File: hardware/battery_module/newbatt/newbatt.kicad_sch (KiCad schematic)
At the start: 28 parts, among them J1 54-00164, J2 Conn_01x10, U1 BQ24210DQCR

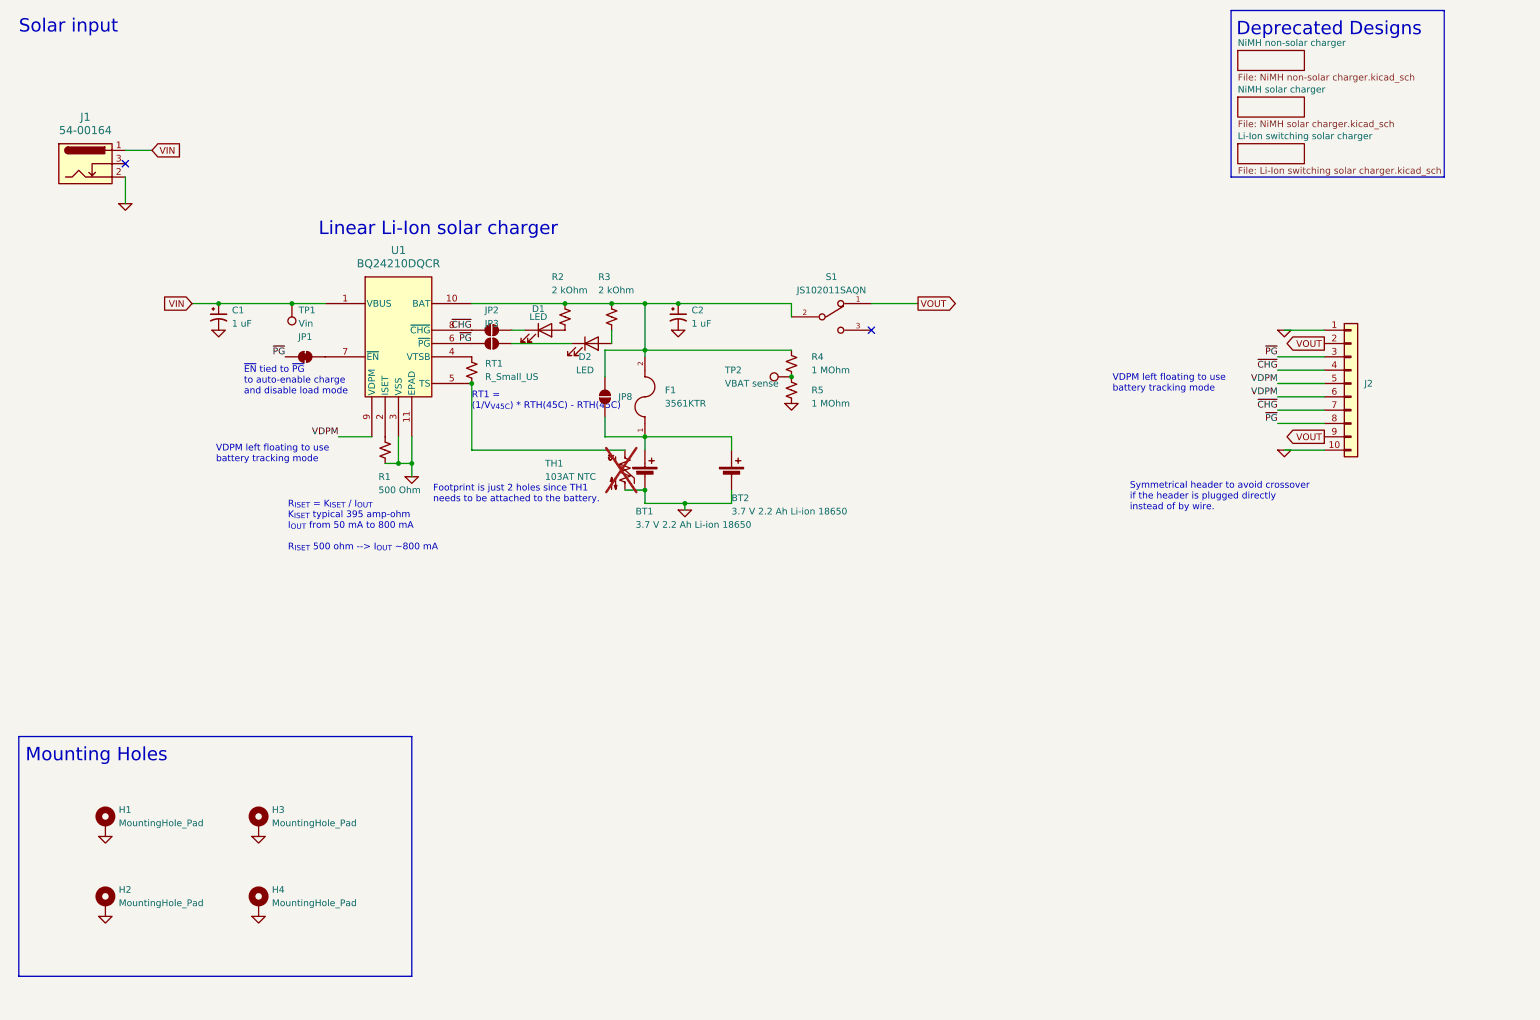
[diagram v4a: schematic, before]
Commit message: Updated BoM with LCSC, Digikey. Updated 18650 battery clip footprint with 67.2mm spacing for 65mm and 67mm cells
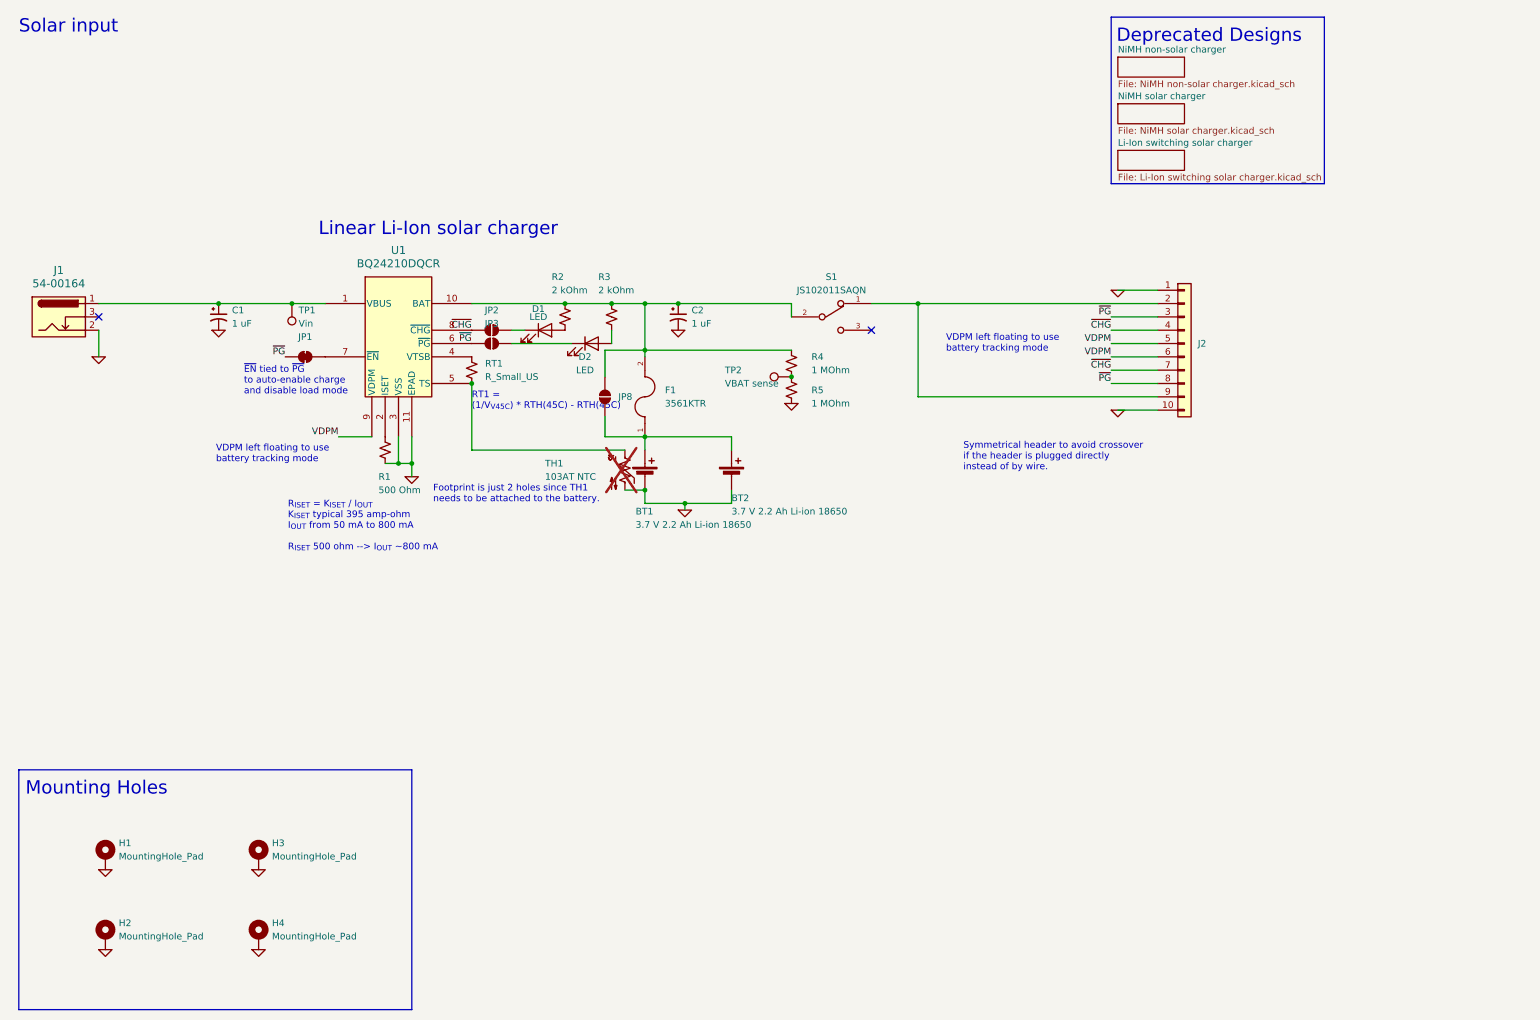
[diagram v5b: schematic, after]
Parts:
- BT1, BT2: footprint Keystone254TR:BAT_254TR -> Keystone254TR:BAT_254TR_67mm; Digikey (none) -> 36-254TR-ND; LCSC (none) -> C5498533; MFC (none) -> Keystone; MPN (none) -> 254TR; QTY (none) -> 4; REF (none) -> BT1, BT2
- F1: Digikey (none) -> 36-3561KTR-ND; LCSC (none) -> C3205939; MFC (none) -> Keystone; MPN (none) -> 3561KTR; QTY (none) -> 1; REF (none) -> F1
- J1: Digikey (none) -> 839-54-00164TR-ND; MFC (none) -> Tensility; MPN (none) -> 54-00164; QTY (none) -> 1; REF (none) -> J1
- J2: Digikey (none) -> S5485-ND; LCSC (none) -> C7327804; MFC (none) -> Sullins Connector Solutions; MPN (none) -> PPPC101LGBN-RC; QTY (none) -> 1; REF (none) -> J2
- S1: Digikey (none) -> 401-1999-2-ND; LCSC (none) -> C221660; MFC (none) -> C&K Switches; MPN (none) -> JS102011SAQN; QTY (none) -> 1; REF (none) -> S1
- TH1: Digikey (none) -> 4316-103AT-4-70374-ND; LCSC (none) -> C20583168; MFC (none) -> Semitec; MPN (none) -> 103AT-4-70374; QTY (none) -> 1; REF (none) -> TH1
- U1: Digikey (none) -> 296-BQ24210DQCRTR-ND; LCSC (none) -> C524795; MFC (none) -> Texas Instruments; MPN (none) -> BQ24210DQCR; QTY (none) -> 1; REF (none) -> U1
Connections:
- net VIN: no longer names the net of C1.1, J1.1, TP1.1, U1.1 (VBUS)
- net VOUT: no longer names the net of J2.2 (Pin_2), J2.9 (Pin_9), S1.1
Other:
- title: (none) -> ENTS Node Battery Module
- moved on the sheet: H1, H2, H3, H4, J1, J2

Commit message: Reviewed with John, updated VDPM and resistor values and barrel jack
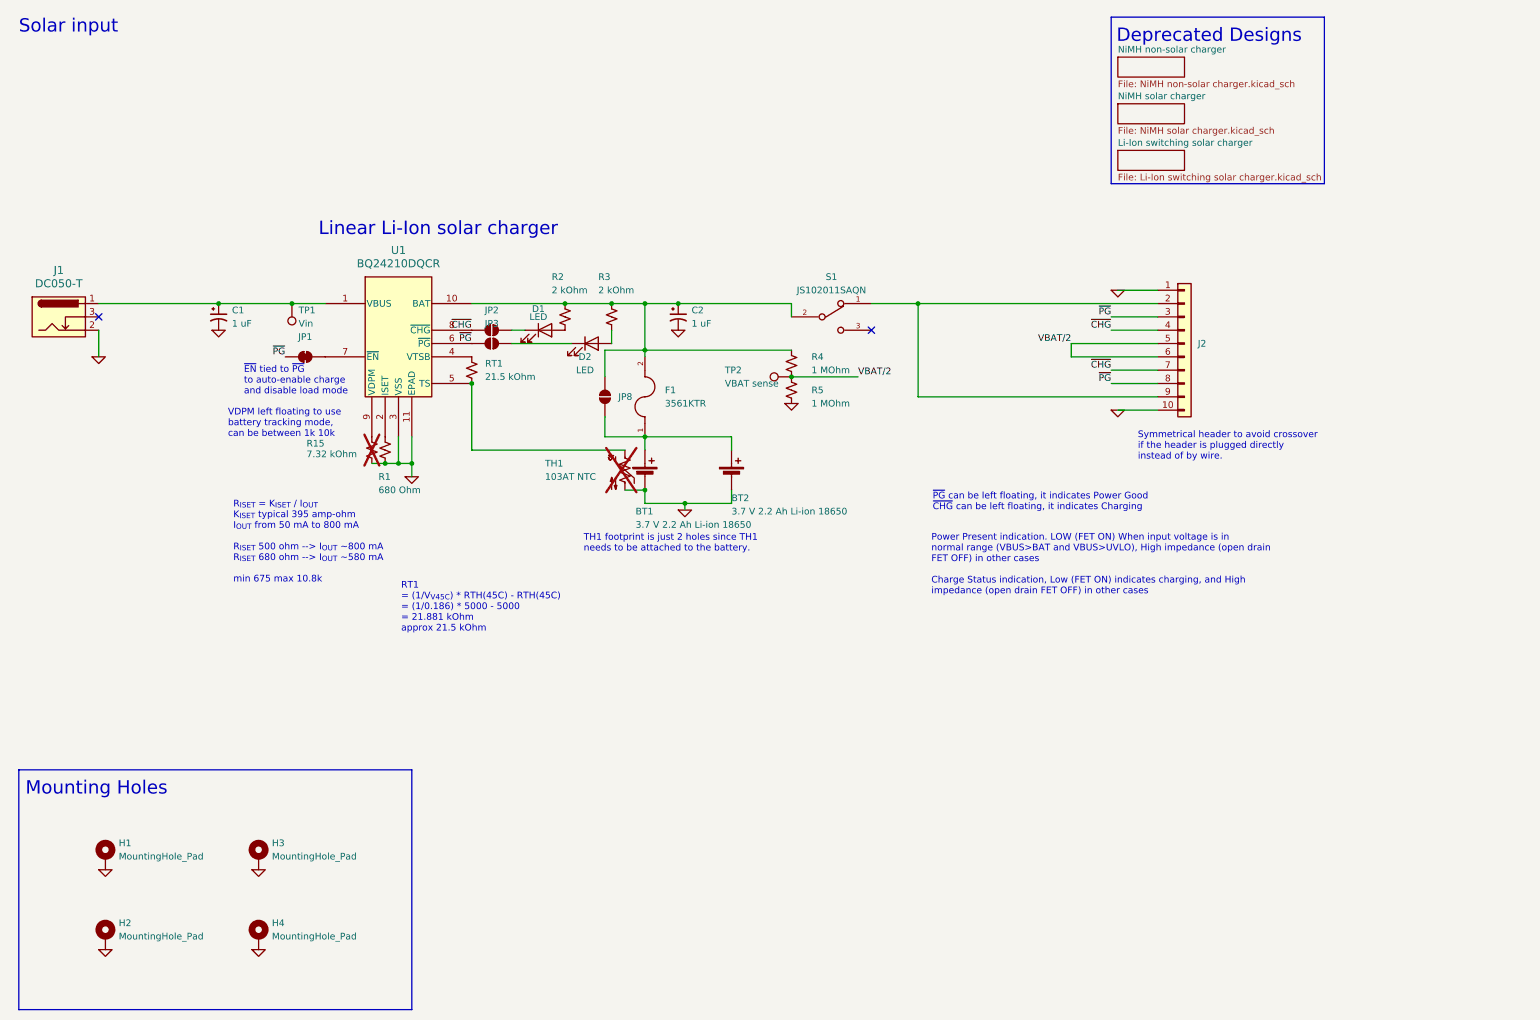
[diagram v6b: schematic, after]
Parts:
- added R15: 7.32 kOhm, Resistor_SMD:R_0603_1608Metric, symbol Device:R_Small_US
- F1: QTY 1 -> 2
- J1: value 54-00164 -> DC050-T; footprint 54-00164:TENSILITY_54-00164 -> DC050-T:DC050-T; symbol 54-00164:54-00164 -> Connector:Barrel_Jack_Switch; Digikey 839-54-00164TR-ND -> (none); LCSC (none) -> C431534; MFC Tensility -> Shou Han; MPN 54-00164 -> DC050-T
- R1: value 500 Ohm -> 680 Ohm
- RT1: value R_Small_US -> 21.5 kOhm
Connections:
- net 0: now also R15.2
- net VBAT/2: now reaches R4.2, R5.1, TP2.1
- net VBAT/2: now also J2.5 (Pin_5), J2.6 (Pin_6)
- removed net VDPM: J2.5 (Pin_5), J2.6 (Pin_6), U1.9 (VDPM)
- new net: R15.1, U1.9 (VDPM)
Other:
- note added: "Power Present indication. LOW (FET ON) When input voltage is in normal range (VBUS>BAT and VBUS>UVLO), High impedance (open drain FET OFF) in other cases Charge Status indication, Low (FET ON) indicates charging, and High impedance (open drain FET OFF) in other cases"
- note added: "RT1 = (1/V_{V45C}) * RTH(45C) - RTH(45C) = (1/0.186) * 5000 - 5000 = 21.881 kOhm approx 21.5 kOhm"
- note added: "R_{ISET} = K_{ISET} / I_{OUT} K_{ISET} typical 395 amp-ohm I_{OUT} from 50 mA to 800 mA R_{ISET} 500 ohm --> I_{OUT} ~800 mA R_{ISET} 680 ohm --> I_{OUT} ~580 mA min 675 max 10.8k"
- note added: "TH1 footprint is just 2 holes since TH1 needs to be attached to the battery."
- note added: "VDPM left floating to use battery tracking mode, can be between 1k 10k"
- note added: "~{PG} can be left floating, it indicates Power Good ~{CHG} can be left floating, it indicates Charging"
- note removed: "Footprint is just 2 holes since TH1 needs to be attached to the battery."
- note removed: "RT1 = (1/V_{V45C}) * RTH(45C) - RTH(45C)"
- note removed: "R_{ISET} = K_{ISET} / I_{OUT} K_{ISET} typical 395 amp-ohm I_{OUT} from 50 mA to 800 mA R_{ISET} 500 ohm --> I_{OUT} ~800 mA"
- note removed: "VDPM left floating to use battery tracking mode"

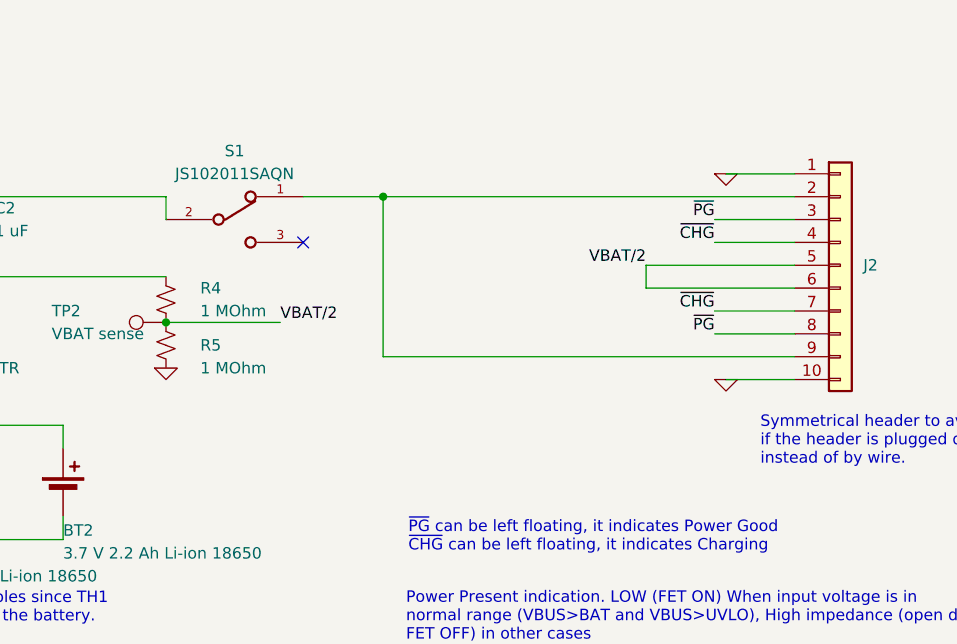
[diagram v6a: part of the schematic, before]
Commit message: Added 3.3V linear regulator
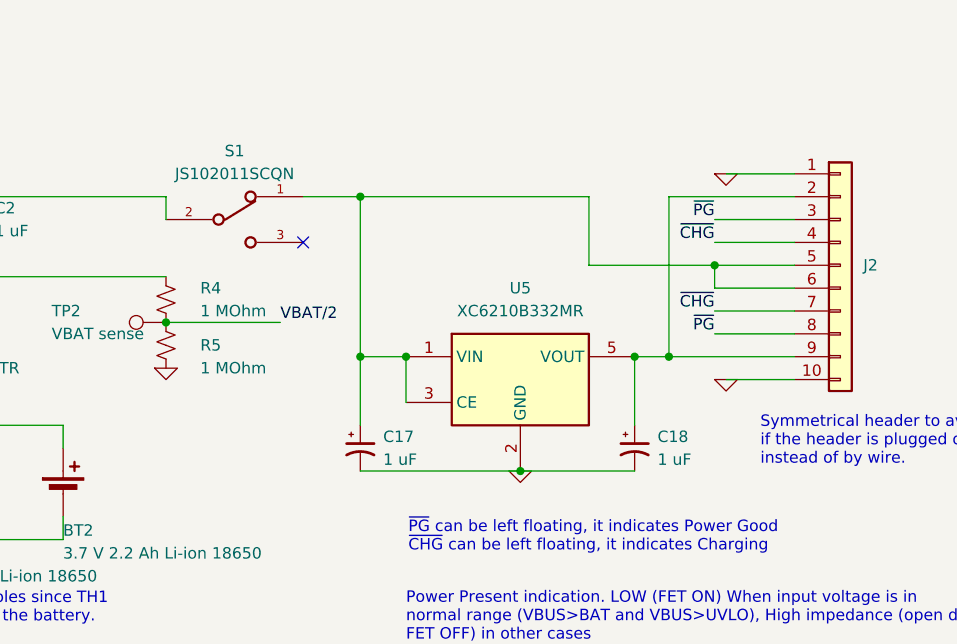
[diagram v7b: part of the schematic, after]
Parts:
- added C17, C18: 1 uF, Capacitor_SMD:C_0603_1608Metric, symbol Device:C_Polarized_Small_US
- added U5: XC6210B332MR, Package_TO_SOT_SMD:SOT-23-5, symbol Regulator_Linear:XC6210B332MR
- S1: value JS102011SAQN -> JS102011SCQN; footprint JS102011SAQN:SW_JS102011SAQN -> JS102011SCQN:SWITCH_1SCQN
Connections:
- net 0: now also C17.2, C18.2, U5.2 (GND)
- net VBAT/2: no longer J2.5 (Pin_5), J2.6 (Pin_6)
- net at J2.2 (Pin_2), J2.9 (Pin_9): now also C18.1, U5.5 (VOUT); no longer S1.1
- new net: C17.1, J2.5 (Pin_5), J2.6 (Pin_6), S1.1, U5.1 (VIN), U5.3 (CE)

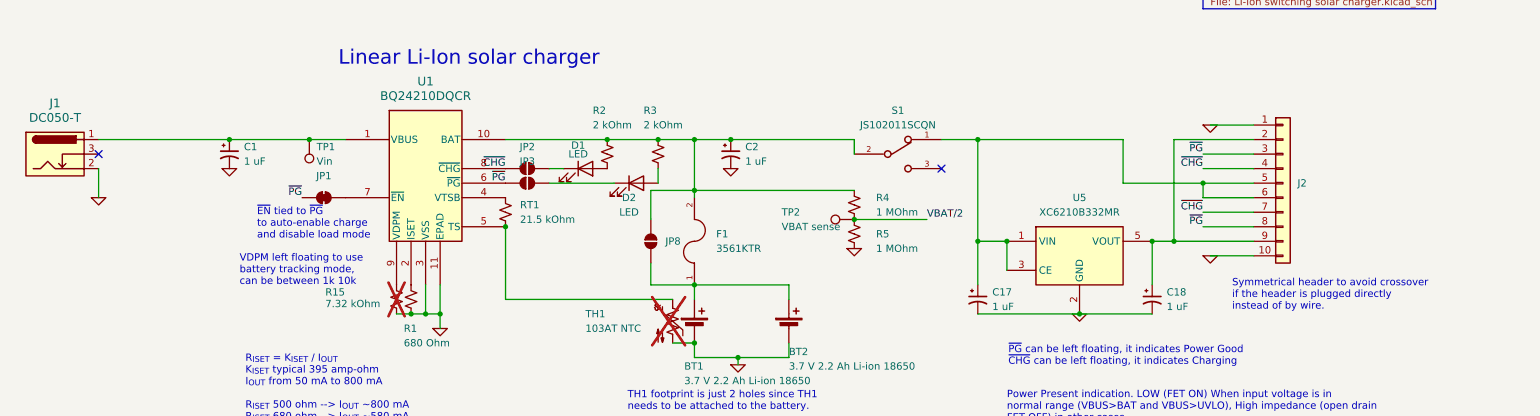
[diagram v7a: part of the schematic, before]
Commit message: 1x10 pin header --> 5 pin JST
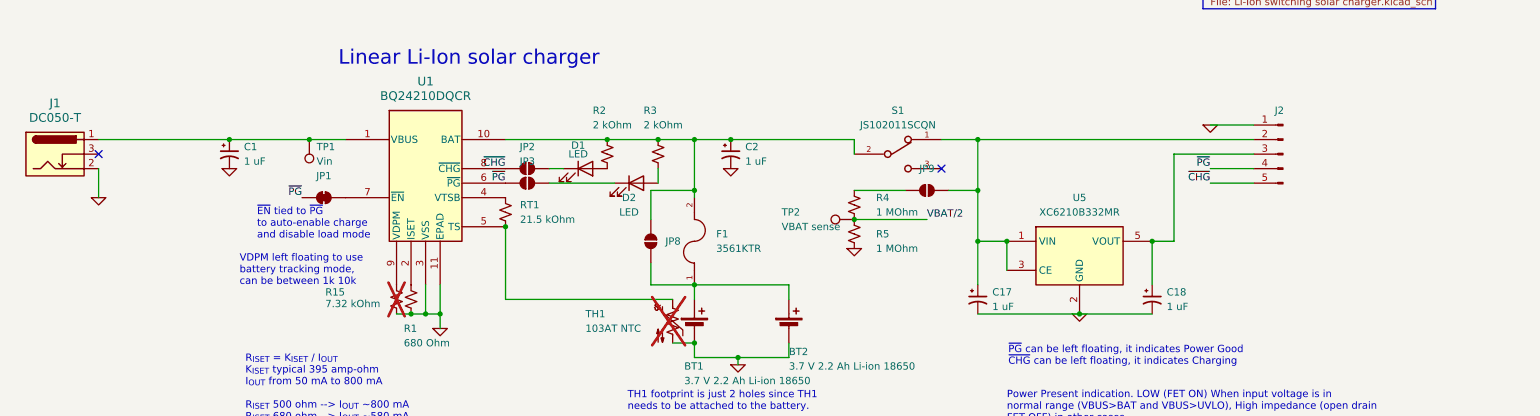
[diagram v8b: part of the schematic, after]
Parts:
- added JP9: SolderJumper_2_Open, Jumper:SolderJumper-2_P1.3mm_Open_RoundedPad1.0x1.5mm, symbol Jumper:SolderJumper_2_Open
- J2: value Conn_01x10 -> Conn_01x05_Pin; footprint Connector_PinSocket_2.54mm:PinSocket_1x10_P2.54mm_Horizontal -> Connector_JST:JST_PH_S5B-PH-SM4-TB_1x05-1MP_P2.00mm_Horizontal; symbol Connector_Generic:Conn_01x10 -> Connector:Conn_01x05_Pin
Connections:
- net 0: no longer J2.10 (Pin_10)
- net ~{CHG}: now also J2.5 (Pin_5); no longer J2.4 (Pin_4), J2.7 (Pin_7)
- net ~{PG}: now also J2.4 (Pin_4); no longer J2.3 (Pin_3), J2.8 (Pin_8)
- net at C2.1, F1.2, JP8.2 (B)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: no longer R4.1
- net at C17.1, S1.1, U5.1 (VIN)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: now also J2.2 (Pin_2), JP9.2 (B); no longer J2.5 (Pin_5), J2.6 (Pin_6)
- net at C18.1, U5.5 (VOUT): now also J2.3 (Pin_3); no longer J2.2 (Pin_2), J2.9 (Pin_9)
- new net: JP9.1 (A), R4.1
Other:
- note removed: "Symmetrical header to avoid crossover if the header is plugged directly instead of by wire."
